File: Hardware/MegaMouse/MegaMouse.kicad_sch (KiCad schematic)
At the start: 6 parts

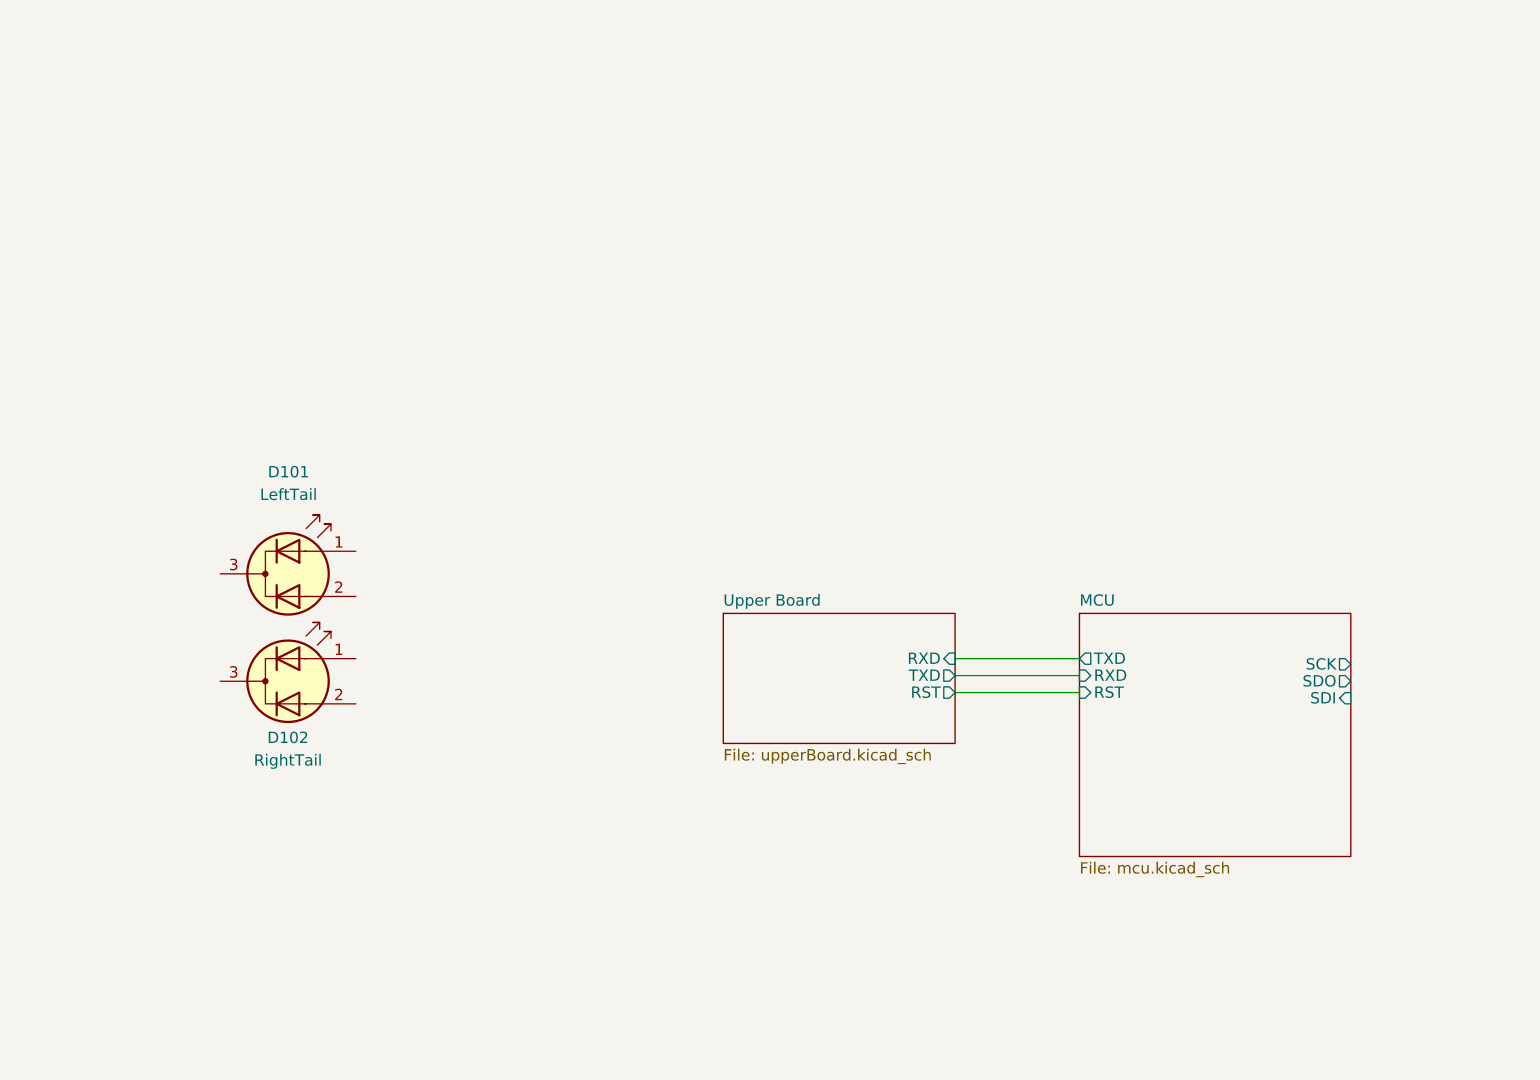
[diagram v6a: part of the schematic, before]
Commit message: Throw on second layer and target a v1.0
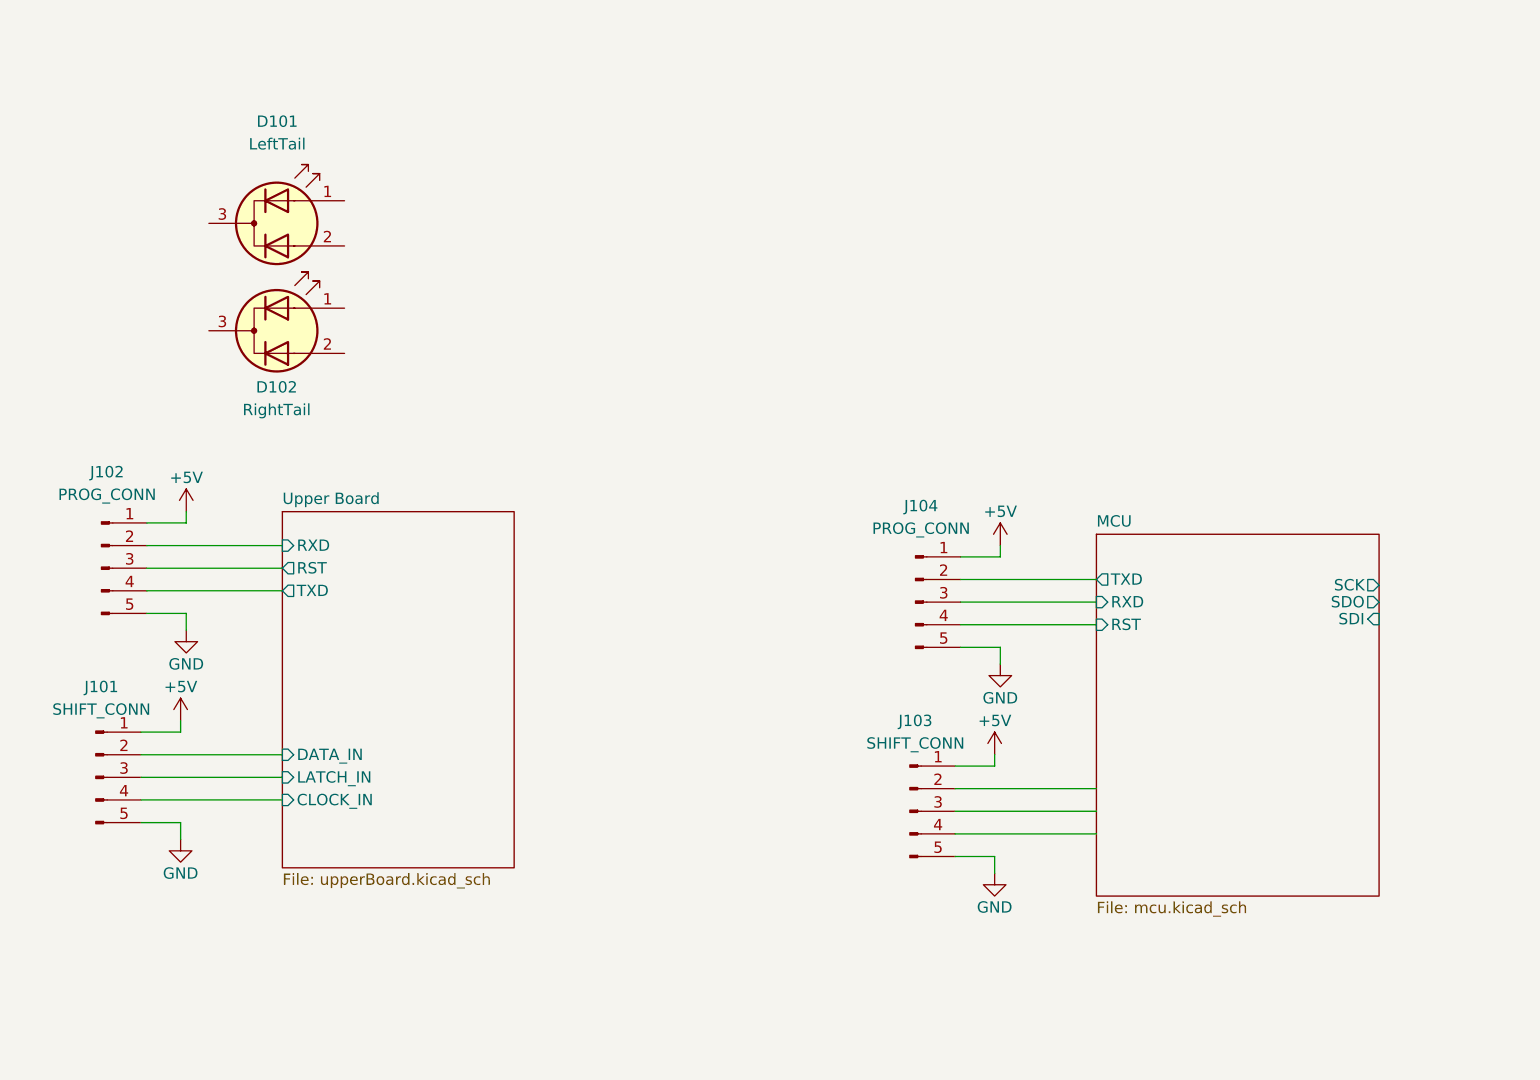
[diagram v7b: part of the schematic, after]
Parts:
- added J101: SHIFT_CONN, Connector_PinHeader_2.54mm:PinHeader_1x05_P2.54mm_Vertical, symbol Connector:Conn_01x05_Male
- added J102: PROG_CONN, Connector_PinHeader_2.54mm:PinHeader_1x05_P2.54mm_Vertical, symbol Connector:Conn_01x05_Male
- added J103: SHIFT_CONN, Connector_PinSocket_2.54mm:PinSocket_1x05_P2.54mm_Vertical, symbol Connector:Conn_01x05_Male
- added J104: PROG_CONN, Connector_PinSocket_2.54mm:PinSocket_1x05_P2.54mm_Vertical, symbol Connector:Conn_01x05_Male
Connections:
- net GND: now also J101.5 (Pin_5), J102.5 (Pin_5), J103.5 (Pin_5), J104.5 (Pin_5)
- net MCU/RST: now also J104.4 (Pin_4)
- net MCU/RXD: now also J104.3 (Pin_3)
- net MCU/TXD: now also J104.2 (Pin_2)
- new net +5V: J101.1 (Pin_1), J102.1 (Pin_1), J103.1 (Pin_1), J104.1 (Pin_1)
- new net Upper Board/CLOCK_IN: J101.4 (Pin_4)
- new net Upper Board/DATA_IN: J101.2 (Pin_2)
- new net Upper Board/LATCH_IN: J101.3 (Pin_3)
- new net Upper Board/RST: J102.3 (Pin_3)
- new net Upper Board/RXD: J102.2 (Pin_2)
- new net Upper Board/TXD: J102.4 (Pin_4)
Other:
- sheet Upper Board ports: added CLOCK_IN, DATA_IN, LATCH_IN; removed none
- moved on the sheet: D101, D102

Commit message: Even more stuff! also bump libs
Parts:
- added R101, R102, R103, R104: 1K, Resistor_SMD:R_0805_2012Metric, symbol Device:R_Small
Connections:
- net GND: now also D101.3 (K), D102.3 (K)
- net at D102.1 (A1): now also R103.1
- net at D102.2 (A2): now also R104.1
- net at D101.1 (A1): now also R101.1
- net at D101.2 (A2): now also R102.1
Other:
- sheet LeftMotor ports: added EncA, EncB, IN1, IN2; removed none
- sheet MCU ports: added none; removed SCK, SDI, SDO
- sheet RightMotor ports: added EncA, EncB, IN1, IN2; removed none
